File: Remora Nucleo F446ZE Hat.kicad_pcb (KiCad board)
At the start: 2 copper layers, 70 x 112 mm, 57 parts, among them J12 NucleoF446ZE CN11 Header, J13 NucleoF446ZE CN12 Header, U10 TPS5430DDAR, U12 HT26LS31ARZ, U13 HT26LS31ARZ, U14 HT26LS31ARZ, U2 TPS5430DDAR, U3 ADuM1201AR, U4 ADuM1201AR, U5 ADuM1201AR, U6 ADuM1201AR, U7 ADuM1201AR, U8 ADuM1201AR, U9 TPS5430DDAR

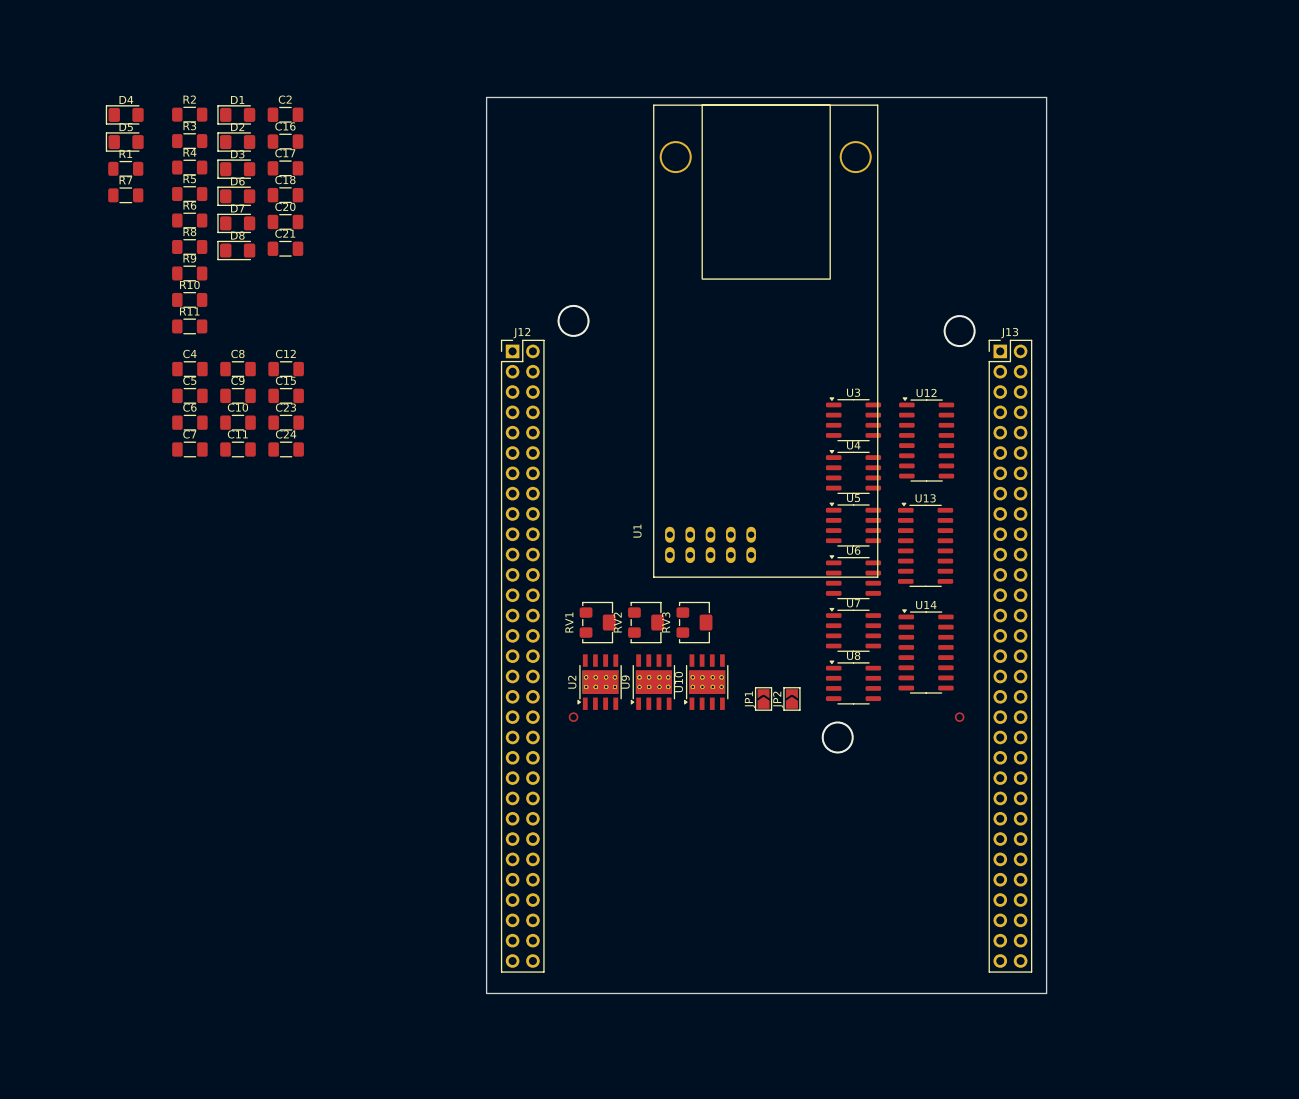
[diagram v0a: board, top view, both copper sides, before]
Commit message: tweaked board edge cuts, mouting hole positions and pin headers to match mechanical drawing. Yet to validate with physical hardware
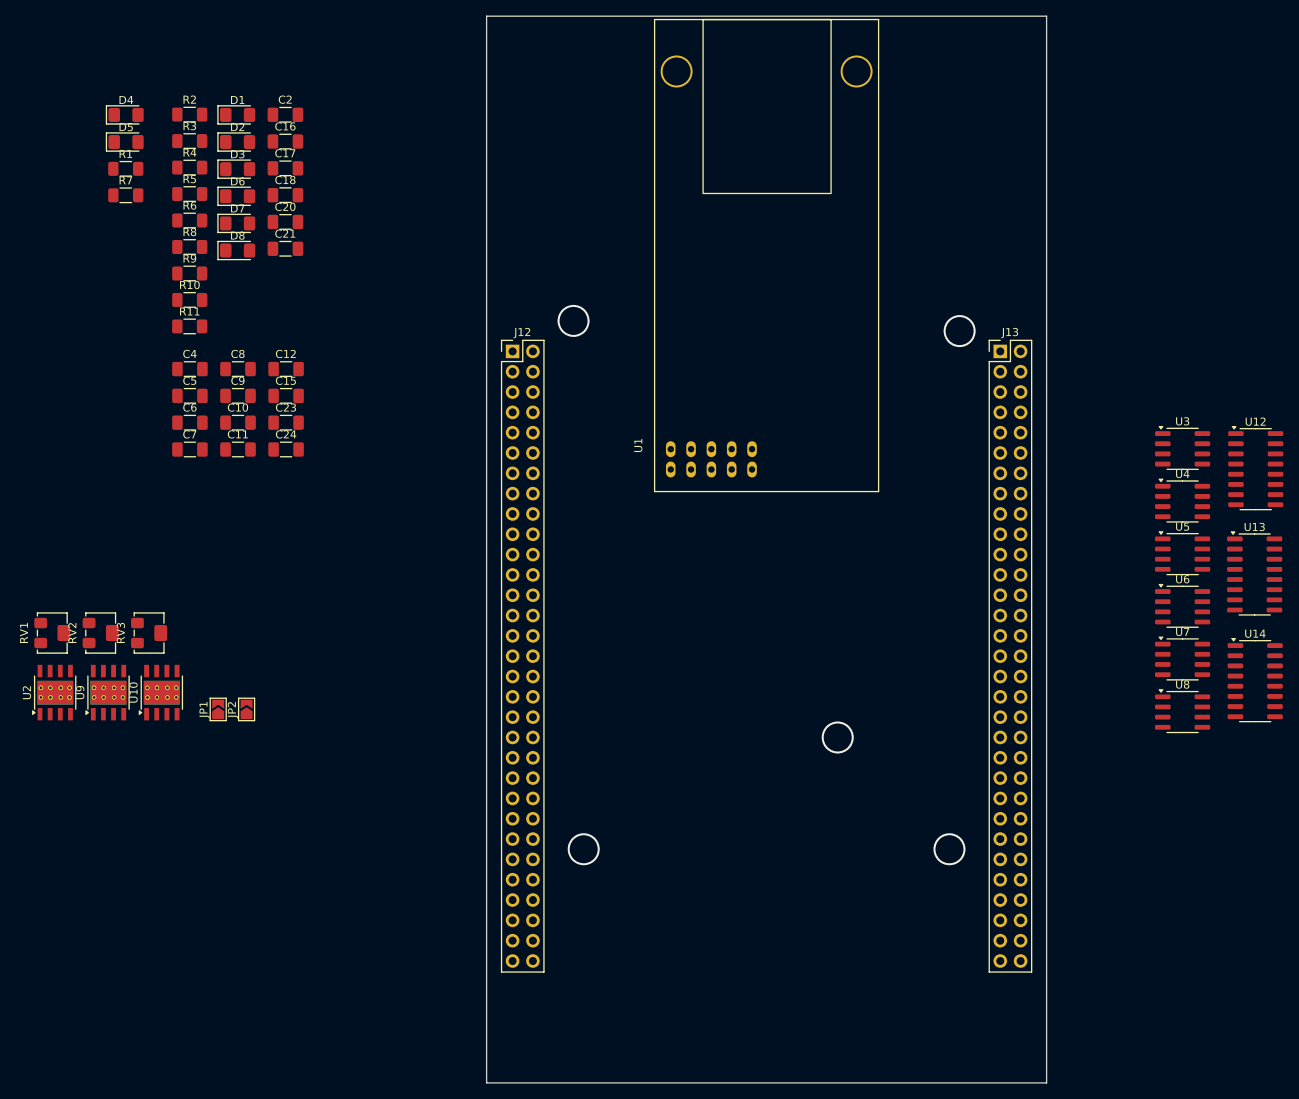
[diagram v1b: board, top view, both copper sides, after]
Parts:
- moved RV2 68.2 mm to (51.8, 116.9)
- moved JP1 68.2 mm to (66.5, 126.5)
- moved RV3 68.2 mm to (57.8, 116.9)
- moved U10 68.2 mm to (59.4, 124.4)
- moved U2 68.2 mm to (46.1, 124.4)
- moved JP2 68.2 mm to (70.0, 126.5)
- moved RV1 68.2 mm to (45.7, 116.9)
- moved U9 68.2 mm to (52.7, 124.4)
- moved U12 41.3 mm to (196.1, 96.5)
- moved U13 41.3 mm to (196.0, 109.6)
- moved U14 41.3 mm to (196.1, 123.0)
- moved U3 41.3 mm to (187.0, 93.9)
- moved U4 41.3 mm to (187.0, 100.5)
- moved U5 41.3 mm to (187.0, 107.1)
- moved U6 41.3 mm to (187.0, 113.7)
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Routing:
- net GNDREF: vias 3 -> 5
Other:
- board size 70 x 112 mm -> 70 x 133.3 mm
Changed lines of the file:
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@@
 	(footprint "Package_SO:SOIC-16_3.9x9.9mm_P1.27mm"
 		(layer "F.Cu")
-		(at 154.94 119.38)
+		(at 196.075 122.96)
 		(descr "SOIC, 16 Pin (JEDEC MS-012, variation AC, https://www.jedec.org/document_search?search_api_views_fulltext=MS-012, https://www.analog.com/media/en/package-pcb-resources/package/pkg_pdf/soic_narrow-r/r_16.pdf), generated with kicad-footprint-generator ipc_gullwing_generator.py")
 		(tags "SOIC SO 16-pin-NSOP R-16 R-16-S D0016A M2B SO16 SOT109-1 751B SOIC_N narrow")
@@
 	(footprint "Package_SO:TI_SO-PowerPAD-8_ThermalVias"
 		(layer "F.Cu")
-		(at 127.575 123.085 90)
+		(at 59.405 124.395 90)
 		(descr "8-pin HTSOP package with 1.27mm pin pitch, compatible with SOIC-8, 3.9x4.9mm² body, exposed pad, thermal vias with large copper area, as proposed in http://www.ti.com/lit/ds/symlink/tps5430.pdf")
 		(tags "HTSOP 1.27")
@@
 	(footprint "Package_SO:TI_SO-PowerPAD-8_ThermalVias"
 		(layer "F.Cu")
-		(at 114.245 123.085 90)
+		(at 46.075 124.395 90)
 		(descr "8-pin HTSOP package with 1.27mm pin pitch, compatible with SOIC-8, 3.9x4.9mm² body, exposed pad, thermal vias with large copper area, as proposed in http://www.ti.com/lit/ds/symlink/tps5430.pdf")
 		(tags "HTSOP 1.27")
@@
 	(footprint "Package_SO:SOIC-8_3.9x4.9mm_P1.27mm"
 		(layer "F.Cu")
-		(at 145.865 90.34)
+		(at 187 93.92)
 		(descr "SOIC, 8 Pin (JEDEC MS-012AA, https://www.analog.com/media/en/package-pcb-resources/package/pkg_pdf/soic_narrow-r/r_8.pdf), generated with kicad-footprint-generator ipc_gullwing_generator.py")
 		(tags "SOIC SO")
@@
 	(footprint "Potentiometer_SMD:Potentiometer_Bourns_3224W_Vertical"
 		(layer "F.Cu")
-		(at 119.93 115.635 90)
+		(at 51.76 116.945 90)
 		(descr "Potentiometer, vertical, Bourns 3224W, https://www.bourns.com/docs/Product-Datasheets/3224.pdf")
 		(tags "Potentiometer vertical Bourns 3224W")
@@
 	(footprint "Package_SO:SOIC-8_3.9x4.9mm_P1.27mm"
 		(layer "F.Cu")
-		(at 145.865 96.92)
+		(at 187 100.5)
 		(descr "SOIC, 8 Pin (JEDEC MS-012AA, https://www.analog.com/media/en/package-pcb-resources/package/pkg_pdf/soic_narrow-r/r_8.pdf), generated with kicad-footprint-generator ipc_gullwing_generator.py")
 		(tags "SOIC SO")
@@
 	(footprint "Package_SO:SOIC-8_3.9x4.9mm_P1.27mm"
 		(layer "F.Cu")
-		(at 145.865 103.5)
+		(at 187 107.08)
 		(descr "SOIC, 8 Pin (JEDEC MS-012AA, https://www.analog.com/media/en/package-pcb-resources/package/pkg_pdf/soic_narrow-r/r_8.pdf), generated with kicad-footprint-generator ipc_gullwing_generator.py")
 		(tags "SOIC SO")
@@
 	(footprint "Package_SO:SOIC-8_3.9x4.9mm_P1.27mm"
 		(layer "F.Cu")
-		(at 145.865 116.66)
+		(at 187 120.24)
 		(descr "SOIC, 8 Pin (JEDEC MS-012AA, https://www.analog.com/media/en/package-pcb-resources/package/pkg_pdf/soic_narrow-r/r_8.pdf), generated with kicad-footprint-generator ipc_gullwing_generator.py")
 		(tags "SOIC SO")
@@
 	(footprint "Jumper:SolderJumper-2_P1.3mm_Open_TrianglePad1.0x1.5mm"
 		(layer "F.Cu")
-		(at 138.17 125.185 90)
+		(at 70 126.495 90)
 		(descr "SMD Solder Jumper, 1x1.5mm Triangular Pads, 0.3mm gap, open")
 		(tags "solder jumper open")
@@
 	(footprint "W5500EvalModule:W5500EvalModule"
 		(layer "F.Cu")
-		(at 134.95 81.7)
+		(at 135.06 71)
 		(property "Reference" "U1"
 			(at -16.06 22.5 90)
@@
 	(footprint "Potentiometer_SMD:Potentiometer_Bourns_3224W_Vertical"
 		(layer "F.Cu")
-		(at 125.98 115.635 90)
+		(at 57.81 116.945 90)
 		(descr "Potentiometer, vertical, Bourns 3224W, https://www.bourns.com/docs/Product-Datasheets/3224.pdf")
 		(tags "Potentiometer vertical Bourns 3224W")
@@
 	(footprint "Package_SO:SOIC-16_3.9x9.9mm_P1.27mm"
 		(layer "F.Cu")
-		(at 155.005 92.88)
+		(at 196.14 96.46)
 		(descr "SOIC, 16 Pin (JEDEC MS-012, variation AC, https://www.jedec.org/document_search?search_api_views_fulltext=MS-012, https://www.analog.com/media/en/package-pcb-resources/package/pkg_pdf/soic_narrow-r/r_16.pdf), generated with kicad-footprint-generator ipc_gullwing_generator.py")
 		(tags "SOIC SO 16-pin-NSOP R-16 R-16-S D0016A M2B SO16 SOT109-1 751B SOIC_N narrow")
@@
 	(footprint "Potentiometer_SMD:Potentiometer_Bourns_3224W_Vertical"
 		(layer "F.Cu")
-		(at 113.88 115.635 90)
+		(at 45.71 116.945 90)
 		(descr "Potentiometer, vertical, Bourns 3224W, https://www.bourns.com/docs/Product-Datasheets/3224.pdf")
 		(tags "Potentiometer vertical Bourns 3224W")
@@
 	(footprint "Package_SO:TI_SO-PowerPAD-8_ThermalVias"
 		(layer "F.Cu")
-		(at 120.91 123.085 90)
+		(at 52.74 124.395 90)
 		(descr "8-pin HTSOP package with 1.27mm pin pitch, compatible with SOIC-8, 3.9x4.9mm² body, exposed pad, thermal vias with large copper area, as proposed in http://www.ti.com/lit/ds/symlink/tps5430.pdf")
 		(tags "HTSOP 1.27")
@@
 	(footprint "Jumper:SolderJumper-2_P1.3mm_Open_TrianglePad1.0x1.5mm"
 		(layer "F.Cu")
-		(at 134.62 125.185 90)
+		(at 66.45 126.495 90)
 		(descr "SMD Solder Jumper, 1x1.5mm Triangular Pads, 0.3mm gap, open")
 		(tags "solder jumper open")
@@
 	(footprint "Package_SO:SOIC-8_3.9x4.9mm_P1.27mm"
 		(layer "F.Cu")
-		(at 145.865 110.08)
+		(at 187 113.66)
 		(descr "SOIC, 8 Pin (JEDEC MS-012AA, https://www.analog.com/media/en/package-pcb-resources/package/pkg_pdf/soic_narrow-r/r_8.pdf), generated with kicad-footprint-generator ipc_gullwing_generator.py")
 		(tags "SOIC SO")
@@
 	(footprint "Package_SO:SOIC-16_3.9x9.9mm_P1.27mm"
 		(layer "F.Cu")
-		(at 154.875 106.045)
+		(at 196.01 109.625)
 		(descr "SOIC, 16 Pin (JEDEC MS-012, variation AC, https://www.jedec.org/document_search?search_api_views_fulltext=MS-012, https://www.analog.com/media/en/package-pcb-resources/package/pkg_pdf/soic_narrow-r/r_16.pdf), generated with kicad-footprint-generator ipc_gullwing_generator.py")
 		(tags "SOIC SO 16-pin-NSOP R-16 R-16-S D0016A M2B SO16 SOT109-1 751B SOIC_N narrow")
@@
 	(footprint "Package_SO:SOIC-8_3.9x4.9mm_P1.27mm"
 		(layer "F.Cu")
-		(at 145.865 123.24)
+		(at 187 126.82)
 		(descr "SOIC, 8 Pin (JEDEC MS-012AA, https://www.analog.com/media/en/package-pcb-resources/package/pkg_pdf/soic_narrow-r/r_8.pdf), generated with kicad-footprint-generator ipc_gullwing_generator.py")
 		(tags "SOIC SO")
@@
 		)
 	)
-	(gr_circle
-		(center 159.13 127.46)
-		(end 159.63 127.46)
-		(stroke
-			(width 0.2)
-			(type solid)
-		)
-		(fill no)
-		(layer "F.Cu")
-	)
-	(gr_circle
-		(center 110.87 127.46)
-		(end 111.37 127.46)
-		(stroke
-			(width 0.2)
-			(type solid)
-		)
-		(fill no)
-		(layer "F.Cu")
-	)
 	(gr_rect
-		(start 100 50)
-		(end 170 162)
+		(start 100 39.84)
+		(end 170 173.18)
 		(stroke
 			(width 0.05)
-			(type default)
+			(type solid)
 		)
 		(fill no)
@@
 	)
 	(via
+		(at 157.86 143.97)
+		(size 4)
+		(drill 3.5)
+		(layers "F.Cu" "B.Cu")
+		(free yes)
+		(net 3)
+	)
+	(via
 		(at 110.87 77.93)
 		(size 4)
 		(drill 3.5)
+		(layers "F.Cu" "B.Cu")
+		(free yes)
+		(net 3)
+	)
+	(via
+		(at 112.14 143.97)
+		(size 4)
+		(drill 3.5)

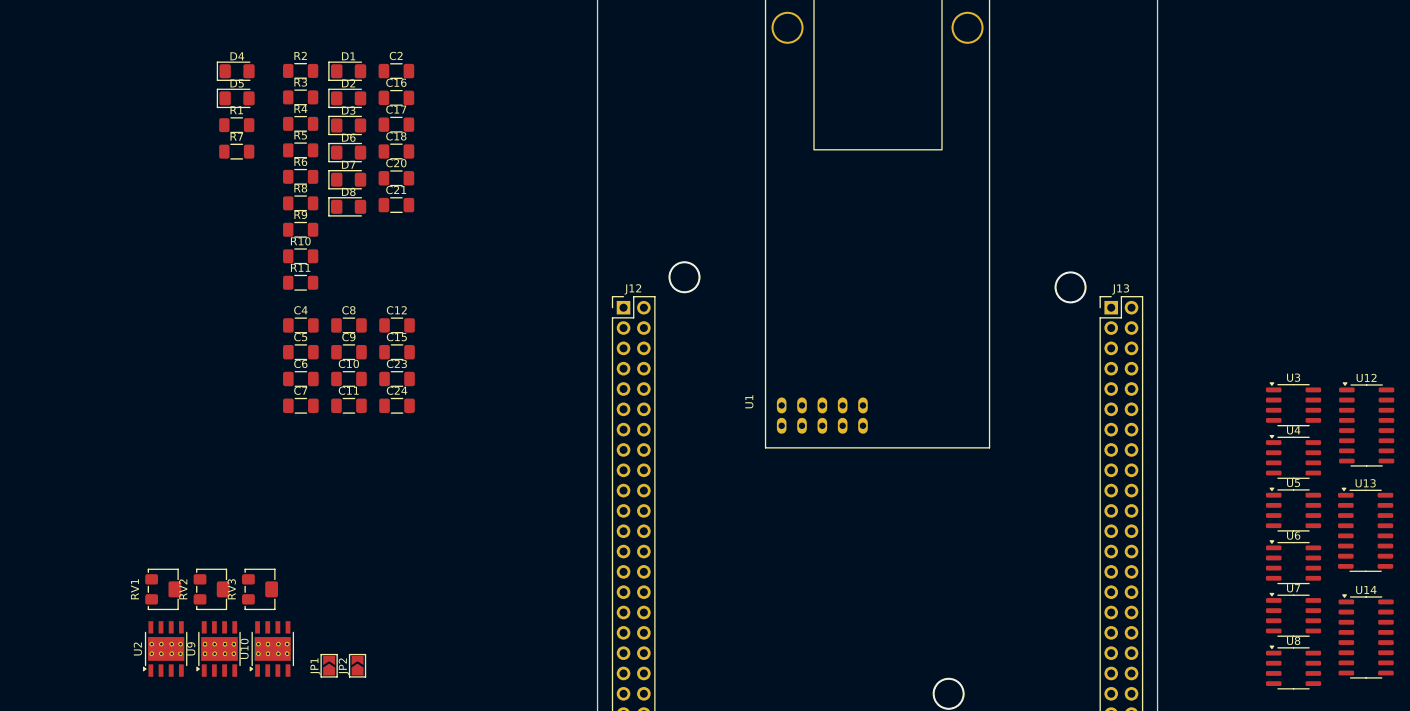
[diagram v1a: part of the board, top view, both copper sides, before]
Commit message: changes some unecessary global labels to local. Added a heirarchical sheet for output driver and basic numbering. Sink logic not yet set for O/Ps, but placeholder for now
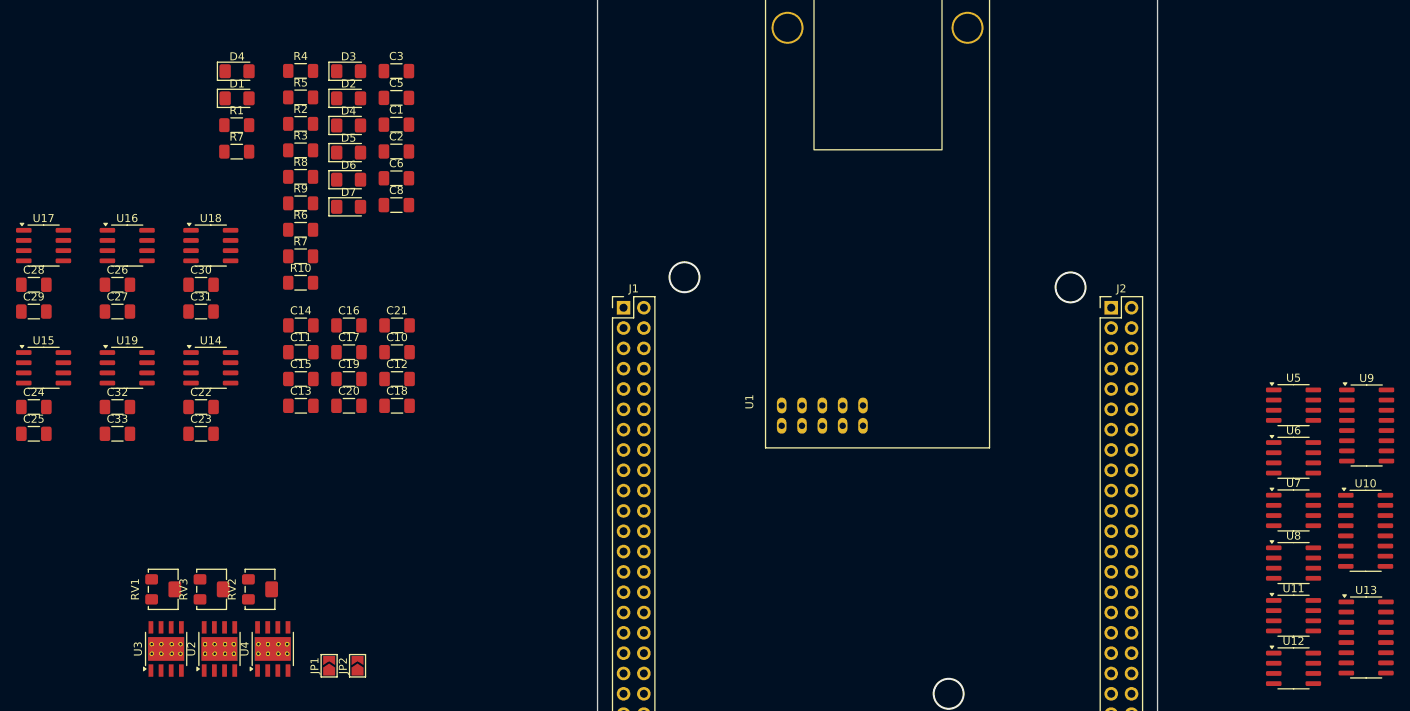
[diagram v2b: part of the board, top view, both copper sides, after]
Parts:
- added C22: 100nF, Capacitor_SMD:C_1206_3216Metric_Pad1.33x1.80mm_HandSolder, F.Cu at (50.4, 94.2)
- added C23: 100nF, Capacitor_SMD:C_1206_3216Metric_Pad1.33x1.80mm_HandSolder, F.Cu at (50.4, 97.5)
- added C24: 100nF, Capacitor_SMD:C_1206_3216Metric_Pad1.33x1.80mm_HandSolder, F.Cu at (29.5, 94.2)
- added C25: 100nF, Capacitor_SMD:C_1206_3216Metric_Pad1.33x1.80mm_HandSolder, F.Cu at (29.5, 97.5)
- added C26: 100nF, Capacitor_SMD:C_1206_3216Metric_Pad1.33x1.80mm_HandSolder, F.Cu at (40.0, 78.9)
- added C27: 100nF, Capacitor_SMD:C_1206_3216Metric_Pad1.33x1.80mm_HandSolder, F.Cu at (40.0, 82.2)
- added C28: 100nF, Capacitor_SMD:C_1206_3216Metric_Pad1.33x1.80mm_HandSolder, F.Cu at (29.5, 78.9)
- added C29: 100nF, Capacitor_SMD:C_1206_3216Metric_Pad1.33x1.80mm_HandSolder, F.Cu at (29.5, 82.2)
- added C30: 100nF, Capacitor_SMD:C_1206_3216Metric_Pad1.33x1.80mm_HandSolder, F.Cu at (50.4, 78.9)
- added C31: 100nF, Capacitor_SMD:C_1206_3216Metric_Pad1.33x1.80mm_HandSolder, F.Cu at (50.4, 82.2)
- added C32: 100nF, Capacitor_SMD:C_1206_3216Metric_Pad1.33x1.80mm_HandSolder, F.Cu at (40.0, 94.2)
- added C33: 100nF, Capacitor_SMD:C_1206_3216Metric_Pad1.33x1.80mm_HandSolder, F.Cu at (40.0, 97.5)
- added U14: ADuM1201AR, Package_SO:SOIC-8_3.9x4.9mm_P1.27mm, F.Cu at (51.7, 89.2)
- added U15: ADuM1201AR, Package_SO:SOIC-8_3.9x4.9mm_P1.27mm, F.Cu at (30.8, 89.2)
- added U16: ADuM1201AR, Package_SO:SOIC-8_3.9x4.9mm_P1.27mm, F.Cu at (41.2, 74.0)
- added U17: ADuM1201AR, Package_SO:SOIC-8_3.9x4.9mm_P1.27mm, F.Cu at (30.8, 74.0)
- added U18: ADuM1201AR, Package_SO:SOIC-8_3.9x4.9mm_P1.27mm, F.Cu at (51.7, 74.0)
- added U19: ADuM1201AR, Package_SO:SOIC-8_3.9x4.9mm_P1.27mm, F.Cu at (41.2, 89.2)
- renumbered C17 to C1, C15 to C10, C5 to C11, C23 to C12, C7 to C13, C4 to C14, C6 to C15, C8 to C16, C9 to C17, C24 to C18, C10 to C19, C18 to C2, C11 to C20, C12 to C21, C2 to C3, C16 to C5, C20 to C6, C21 to C8, D5 to D1, D1 to D3, D3 to D4, D6 to D5, D7 to D6, D8 to D7, J12 to J1, J13 to J2, R11 to R10, R4 to R2, R5 to R3, R2 to R4, R3 to R5, R9 to R6, R10 to R7, R6 to R8, R8 to R9, RV3 to RV2, RV2 to RV3, U13 to U10, U7 to U11, U8 to U12, U14 to U13, U9 to U2, U2 to U3, U10 to U4, U3 to U5, U4 to U6, U5 to U7, U6 to U8, U12 to U9
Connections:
- net SPI1_CLK renamed /SPI1_CLK
- net SPI1_MISO renamed /SPI1_MISO
- net SPI1_MOSI renamed /SPI1_MOSI
- net WIZ_CS renamed /WIZ_CS
- net WIZ_RST renamed /WIZ_RST
- D1 pad 1: UART_TX -> /UART_TX
- J1 pad 1: UART_TX -> unconnected-(J1-Pin_1-Pad1)
- J2 pad 10: unconnected-(J13-Pin_10-Pad10) -> /UART_TX
- J2 pad 6: UART_RX -> unconnected-(J2-Pin_6-Pad6)
- R2 pad 2: VSENSE -> /Regulators/5V_SENSE
- R4 pad 2: VSENSE -> /Regulators/12V_SENSE
- R8 pad 2: VSENSE -> /Regulators/3V3_SENSE
- RV1 pad 1: VSENSE -> /Regulators/5V_SENSE
- RV2 pad 1: VSENSE -> /Regulators/12V_SENSE
- RV3 pad 1: VSENSE -> /Regulators/3V3_SENSE
- U2 pad 4: VSENSE -> /Regulators/5V_SENSE
- U3 pad 4: VSENSE -> /Regulators/12V_SENSE
- U4 pad 4: VSENSE -> /Regulators/3V3_SENSE
